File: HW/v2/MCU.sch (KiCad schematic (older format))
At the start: 19 parts, among them J10 RST, J11 ScopeTest, J12 Trigger BTN, J13 External trigger, J9 GPIO, U12 Bluepill, U13 DS3231 RTC, U14 TRIG, U15 SN74LVC2G14, U16 PC817

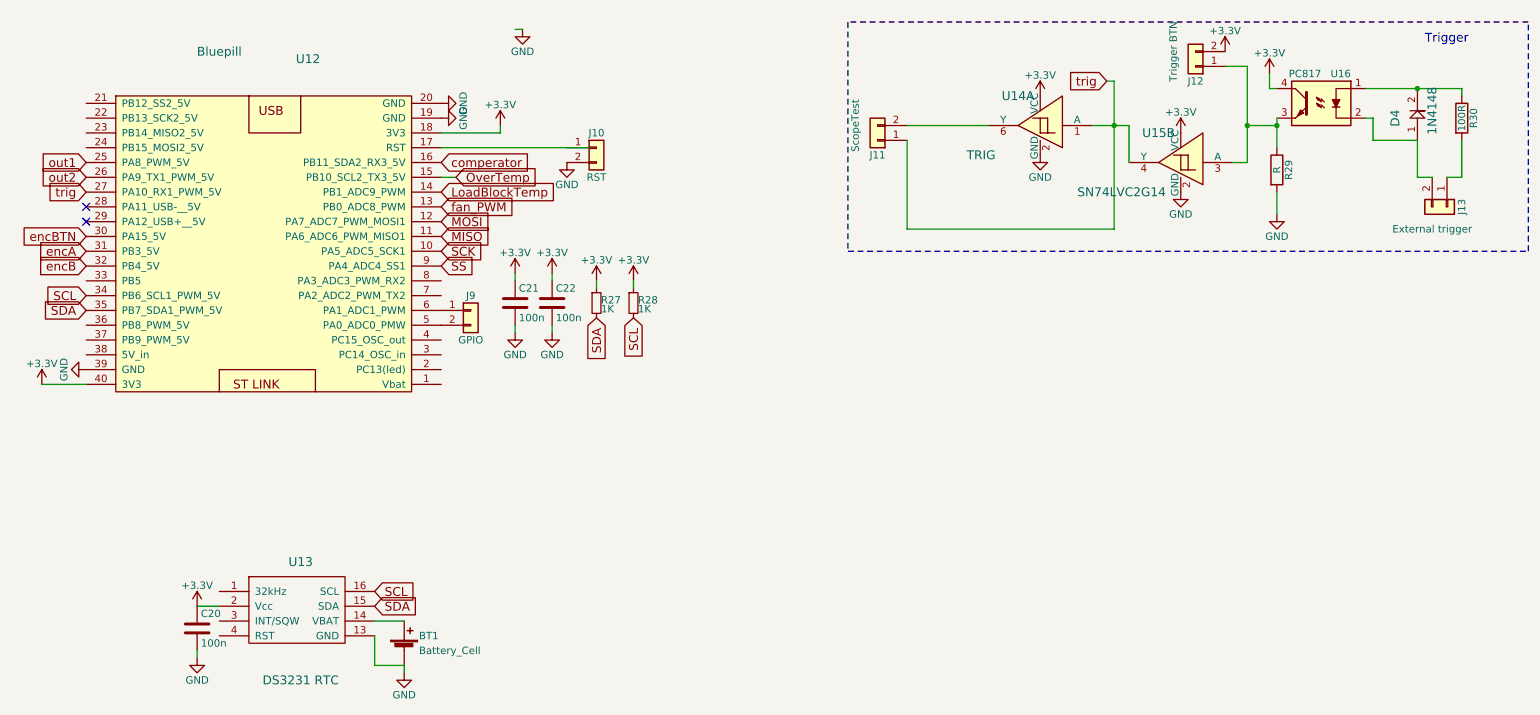
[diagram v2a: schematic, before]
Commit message: i2c pots for calibrating
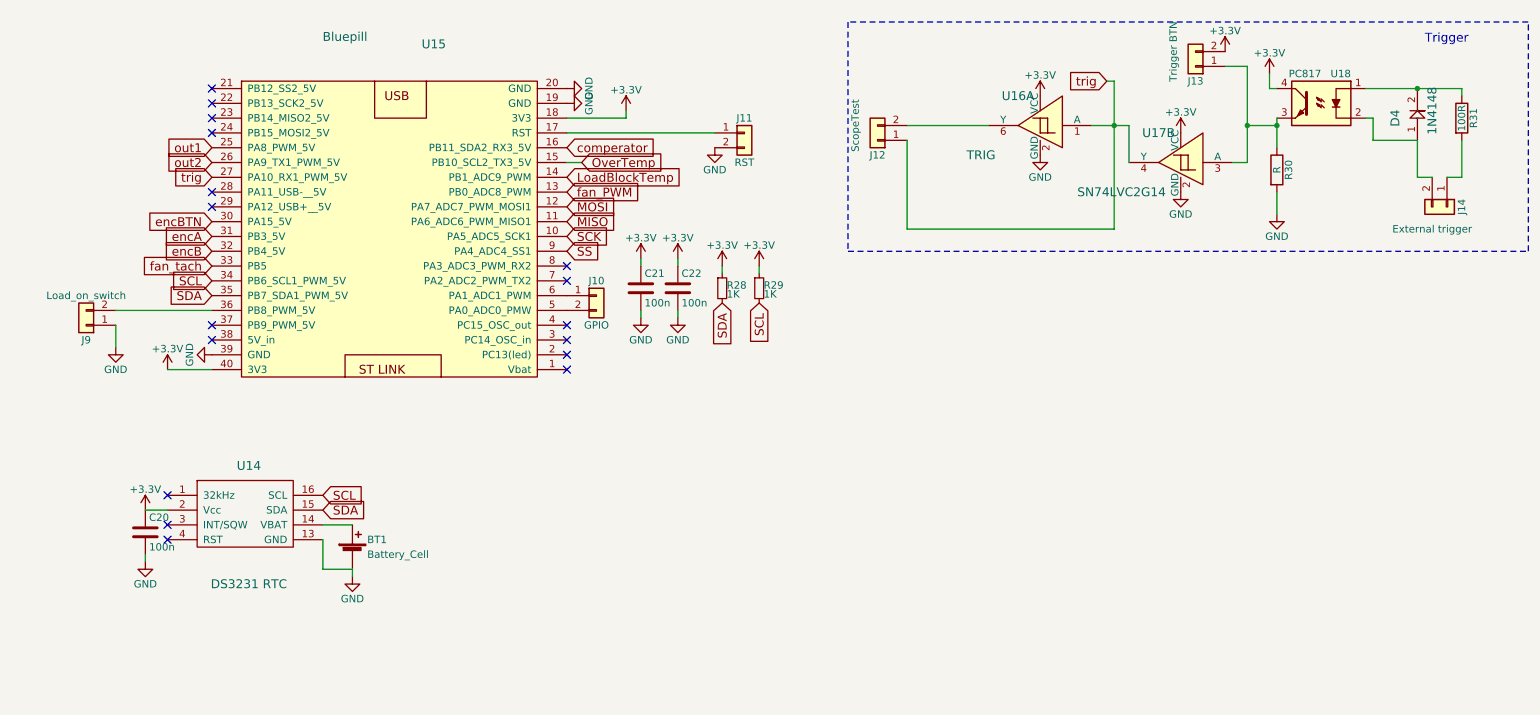
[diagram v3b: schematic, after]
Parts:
- added J9: Load_on_switch, Pin_Headers:Pin_Header_Straight_1x02_Pitch2.54mm, symbol Conn_01x02
- BT1: footprint Battery_Holders:Keystone_3008_1x2450-CoinCell -> Libs:JUMPER_5MM
- renumbered J9 to J10, J10 to J11, J11 to J12, J12 to J13, J13 to J14, R27 to R28, R28 to R29, R29 to R30, R30 to R31, U13 to U14, U12 to U15, U14 to U16, U15 to U17, U16 to U18
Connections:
- net labels added: fan_tach
- wire segments 42 -> 43
- no-connect marks 2 -> 17
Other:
- moved on the sheet: BT1, C20, C21, C22, J10, J11, R28, R29, U14, U15

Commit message: v2 done
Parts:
- U16: renamed from U17; value SN74LVC2G14 -> TRIG
- renumbered C20 to C21, C21 to C22, C22 to C23
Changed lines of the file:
@@
 $EndComp
 $Comp
-L +3.3V #PWR088
+L +3.3V #PWR087
 U 1 1 5ADB71A1
 P 5250 2450
-F 0 "#PWR088" H 5250 2300 50  0001 C CNN
+F 0 "#PWR087" H 5250 2300 50  0001 C CNN
 F 1 "+3.3V" H 5250 2590 50  0000 C CNN
 F 2 "" H 5250 2450 50  0001 C CNN
@@
 $EndComp
 $Comp
-L +3.3V #PWR089
+L +3.3V #PWR088
 U 1 1 5ADB71A7
 P 5500 2450
-F 0 "#PWR089" H 5500 2300 50  0001 C CNN
+F 0 "#PWR088" H 5500 2300 50  0001 C CNN
 F 1 "+3.3V" H 5500 2590 50  0000 C CNN
 F 2 "" H 5500 2450 50  0001 C CNN
@@
 $EndComp
 $Comp
-L GND #PWR090
+L GND #PWR089
 U 1 1 5ADB71AD
 P 1800 3050
-F 0 "#PWR090" H 1800 2800 50  0001 C CNN
+F 0 "#PWR089" H 1800 2800 50  0001 C CNN
 F 1 "GND" H 1800 2900 50  0000 C CNN
 F 2 "" H 1800 3050 50  0001 C CNN
@@
 OverTemp
 $Comp
-L GND #PWR091
+L GND #PWR090
 U 1 1 5ADB71BF
 P 5200 1650
-F 0 "#PWR091" H 5200 1400 50  0001 C CNN
+F 0 "#PWR090" H 5200 1400 50  0001 C CNN
 F 1 "GND" H 5200 1500 50  0000 C CNN
 F 2 "" H 5200 1650 50  0001 C CNN
@@
 $EndComp
 $Comp
-L GND #PWR092
+L GND #PWR091
 U 1 1 5ADB71DD
 P 4200 1250
-F 0 "#PWR092" H 4200 1000 50  0001 C CNN
+F 0 "#PWR091" H 4200 1000 50  0001 C CNN
 F 1 "GND" H 4200 1100 50  0000 C CNN
 F 2 "" H 4200 1250 50  0001 C CNN
@@
 $EndComp
 $Comp
-L GND #PWR093
+L GND #PWR092
 U 1 1 5ADB71E3
 P 4200 1350
-F 0 "#PWR093" H 4200 1100 50  0001 C CNN
+F 0 "#PWR092" H 4200 1100 50  0001 C CNN
 F 1 "GND" H 4200 1200 50  0000 C CNN
 F 2 "" H 4200 1350 50  0001 C CNN
@@
 	4600 1450 4600 1400
 $Comp
-L +3.3V #PWR094
+L +3.3V #PWR093
 U 1 1 5ADB71EB
 P 4600 1400
-F 0 "#PWR094" H 4600 1250 50  0001 C CNN
+F 0 "#PWR093" H 4600 1250 50  0001 C CNN
 F 1 "+3.3V" H 4600 1540 50  0000 C CNN
 F 2 "" H 4600 1400 50  0001 C CNN
@@
 	4950 2450 4950 2400
 $Comp
-L GND #PWR095
+L GND #PWR094
 U 1 1 5ADB71F3
 P 4950 2800
-F 0 "#PWR095" H 4950 2550 50  0001 C CNN
+F 0 "#PWR094" H 4950 2550 50  0001 C CNN
 F 1 "GND" H 4950 2650 50  0000 C CNN
 F 2 "" H 4950 2800 50  0001 C CNN
@@
 $EndComp
 $Comp
-L C C22
+L C C23
 U 1 1 5ADB71F9
 P 4950 2600
-F 0 "C22" H 4975 2700 50  0000 L CNN
+F 0 "C23" H 4975 2700 50  0000 L CNN
 F 1 "100n" H 4975 2500 50  0000 L CNN
 F 2 "Capacitors_SMD:C_0805_HandSoldering" H 4988 2450 50  0001 C CNN
@@
 $EndComp
 $Comp
-L +3.3V #PWR096
+L +3.3V #PWR095
 U 1 1 5ADB7200
 P 4950 2400
-F 0 "#PWR096" H 4950 2250 50  0001 C CNN
+F 0 "#PWR095" H 4950 2250 50  0001 C CNN
 F 1 "+3.3V" H 4950 2540 50  0000 C CNN
 F 2 "" H 4950 2400 50  0001 C CNN
@@
 	4700 2450 4700 2400
 $Comp
-L GND #PWR097
+L GND #PWR096
 U 1 1 5ADB7208
 P 4700 2800
-F 0 "#PWR097" H 4700 2550 50  0001 C CNN
+F 0 "#PWR096" H 4700 2550 50  0001 C CNN
 F 1 "GND" H 4700 2650 50  0000 C CNN
 F 2 "" H 4700 2800 50  0001 C CNN
@@
 $EndComp
 $Comp
-L C C21
+L C C22
 U 1 1 5ADB720E
 P 4700 2600
-F 0 "C21" H 4725 2700 50  0000 L CNN
+F 0 "C22" H 4725 2700 50  0000 L CNN
 F 1 "100n" H 4725 2500 50  0000 L CNN
 F 2 "Capacitors_SMD:C_0805_HandSoldering" H 4738 2450 50  0001 C CNN
@@
 $EndComp
 $Comp
-L +3.3V #PWR098
+L +3.3V #PWR097
 U 1 1 5ADB7215
 P 4700 2400
-F 0 "#PWR098" H 4700 2250 50  0001 C CNN
+F 0 "#PWR097" H 4700 2250 50  0001 C CNN
 F 1 "+3.3V" H 4700 2540 50  0000 C CNN
 F 2 "" H 4700 2400 50  0001 C CNN
@@
 $EndComp
 $Comp
-L +3.3V #PWR099
+L +3.3V #PWR098
 U 1 1 5ADB721B
 P 1500 3150
-F 0 "#PWR099" H 1500 3000 50  0001 C CNN
+F 0 "#PWR098" H 1500 3000 50  0001 C CNN
 F 1 "+3.3V" H 1500 3290 50  0000 C CNN
 F 2 "" H 1500 3150 50  0001 C CNN
@@
 $EndComp
 $Comp
-L GND #PWR0100
+L GND #PWR099
 U 1 1 5ADB847B
 P 9000 2100
-F 0 "#PWR0100" H 9000 1850 50  0001 C CNN
+F 0 "#PWR099" H 9000 1850 50  0001 C CNN
 F 1 "GND" H 9000 1950 50  0000 C CNN
 F 2 "" H 9000 2100 50  0001 C CNN
@@
 $EndComp
 $Comp
-L GND #PWR0101
+L GND #PWR0100
 U 1 1 5ADB8490
 P 8350 1950
-F 0 "#PWR0101" H 8350 1700 50  0001 C CNN
+F 0 "#PWR0100" H 8350 1700 50  0001 C CNN
 F 1 "GND" H 8350 1800 50  0000 C CNN
 F 2 "" H 8350 1950 50  0001 C CNN
@@
 $EndComp
 $Comp
-L GND #PWR0102
+L GND #PWR0101
 U 1 1 5ADB8496
 P 7400 1700
-F 0 "#PWR0102" H 7400 1450 50  0001 C CNN
+F 0 "#PWR0101" H 7400 1450 50  0001 C CNN
 F 1 "GND" H 7400 1550 50  0000 C CNN
 F 2 "" H 7400 1700 50  0001 C CNN
@@
 $EndComp
 $Comp
-L +3.3V #PWR0103
+L +3.3V #PWR0102
 U 1 1 5ADB849C
 P 7400 1300
-F 0 "#PWR0103" H 7400 1150 50  0001 C CNN
+F 0 "#PWR0102" H 7400 1150 50  0001 C CNN
 F 1 "+3.3V" H 7400 1440 50  0000 C CNN
 F 2 "" H 7400 1300 50  0001 C CNN
@@
 $EndComp
 $Comp
-L +3.3V #PWR0104
+L +3.3V #PWR0103
 U 1 1 5ADB84A2
 P 8350 1550
-F 0 "#PWR0104" H 8350 1400 50  0001 C CNN
+F 0 "#PWR0103" H 8350 1400 50  0001 C CNN
 F 1 "+3.3V" H 8350 1690 50  0000 C CNN
 F 2 "" H 8350 1550 50  0001 C CNN
@@
 $EndComp
 $Comp
-L +3.3V #PWR0105
+L +3.3V #PWR0104
 U 1 1 5ADB84A8
 P 8650 1000
-F 0 "#PWR0105" H 8650 850 50  0001 C CNN
+F 0 "#PWR0104" H 8650 850 50  0001 C CNN
 F 1 "+3.3V" H 8650 1140 50  0000 C CNN
 F 2 "" H 8650 1000 50  0001 C CNN
@@
 $EndComp
 $Comp
-L +3.3V #PWR0106
+L +3.3V #PWR0105
 U 1 1 5ADB84AE
 P 8950 1150
-F 0 "#PWR0106" H 8950 1000 50  0001 C CNN
+F 0 "#PWR0105" H 8950 1000 50  0001 C CNN
 F 1 "+3.3V" H 8950 1290 50  0000 C CNN
 F 2 "" H 8950 1150 50  0001 C CNN
@@
 U 1 1 5ADB84D4
 P 7400 1550
-F 0 "U16" H 7550 1800 60  0000 C CNN
+F 0 "U16" H 7100 1450 60  0000 C CNN
 F 1 "TRIG" H 7800 1400 60  0000 C CNN
 F 2 "TO_SOT_Packages_SMD:SOT-23-6_Handsoldering" H 7400 2300 60  0001 C CNN
@@
 $EndComp
 $Comp
-L SN74LVC2G14 U17
+L SN74LVC2G14 U16
 U 2 1 5ADB84DB
 P 8350 1800
-F 0 "U17" H 8500 2050 60  0000 C CNN
-F 1 "SN74LVC2G14" H 8750 1650 60  0000 C CNN
+F 0 "U16" H 8000 1700 60  0000 C CNN
+F 1 "TRIG" H 8750 1650 60  0000 C CNN
 F 2 "TO_SOT_Packages_SMD:SOT-23-6_Handsoldering" H 8350 2550 60  0001 C CNN
 F 3 "http://www.ti.com/lit/ds/symlink/sn74lvc1g14.pdf" H 8350 2400 60  0001 C CNN
@@
 $EndComp
 $Comp
-L GND #PWR0107
+L GND #PWR0106
 U 1 1 5ADB8A78
 P 2750 4550
-F 0 "#PWR0107" H 2750 4300 50  0001 C CNN
+F 0 "#PWR0106" H 2750 4300 50  0001 C CNN
 F 1 "GND" H 2750 4400 50  0000 C CNN
 F 2 "" H 2750 4550 50  0001 C CNN
@@
 SDA
 $Comp
-L +3.3V #PWR0108
+L +3.3V #PWR0107
 U 1 1 5ADB8A87
 P 1350 4100
-F 0 "#PWR0108" H 1350 3950 50  0001 C CNN
+F 0 "#PWR0107" H 1350 3950 50  0001 C CNN
 F 1 "+3.3V" H 1350 4240 50  0000 C CNN
 F 2 "" H 1350 4100 50  0001 C CNN
@@
 $EndComp
 $Comp
-L C C20
+L C C21
 U 1 1 5ADB8A8D
 P 1350 4250
-F 0 "C20" H 1375 4350 50  0000 L CNN
+F 0 "C21" H 1375 4350 50  0000 L CNN
 F 1 "100n" H 1375 4150 50  0000 L CNN
 F 2 "Capacitors_SMD:C_0805_HandSoldering" H 1388 4100 50  0001 C CNN
@@
 $EndComp
 $Comp
-L GND #PWR0109
+L GND #PWR0108
 U 1 1 5ADB8A94
 P 1350 4450
-F 0 "#PWR0109" H 1350 4200 50  0001 C CNN
+F 0 "#PWR0108" H 1350 4200 50  0001 C CNN
 F 1 "GND" H 1350 4300 50  0000 C CNN
 F 2 "" H 1350 4450 50  0001 C CNN
@@
 $EndComp
 $Comp
-L GND #PWR0110
+L GND #PWR0109
 U 1 1 5ADC9FA5
 P 1150 3000
-F 0 "#PWR0110" H 1150 2750 50  0001 C CNN
+F 0 "#PWR0109" H 1150 2750 50  0001 C CNN
 F 1 "GND" H 1150 2850 50  0000 C CNN
 F 2 "" H 1150 3000 50  0001 C CNN
